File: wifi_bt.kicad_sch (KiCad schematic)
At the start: 37 parts, among them J3 U_FL-R-SMT-1, U26 WiFi_Bluetooth_LBEE5PK2AE, Y4 Oscillator_32.768kHz_ECS_2520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

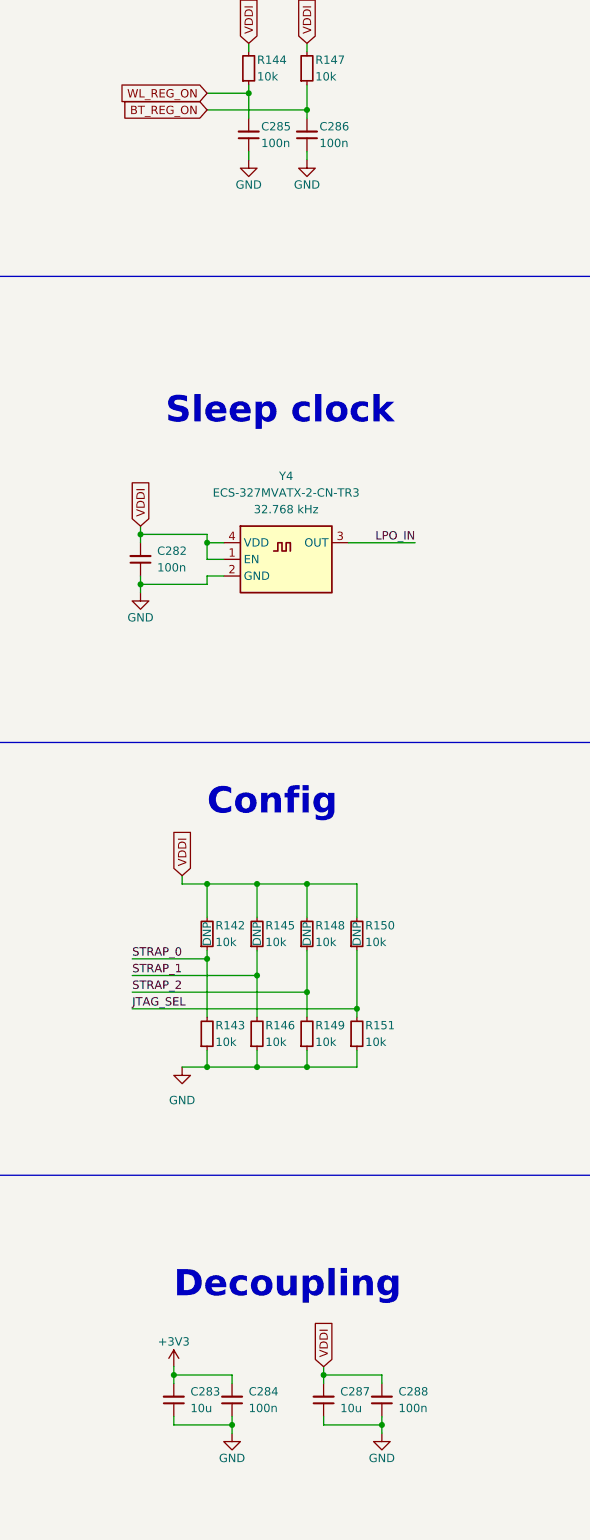
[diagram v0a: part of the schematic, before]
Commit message: [#55992] Move Flash and WL_BT module down
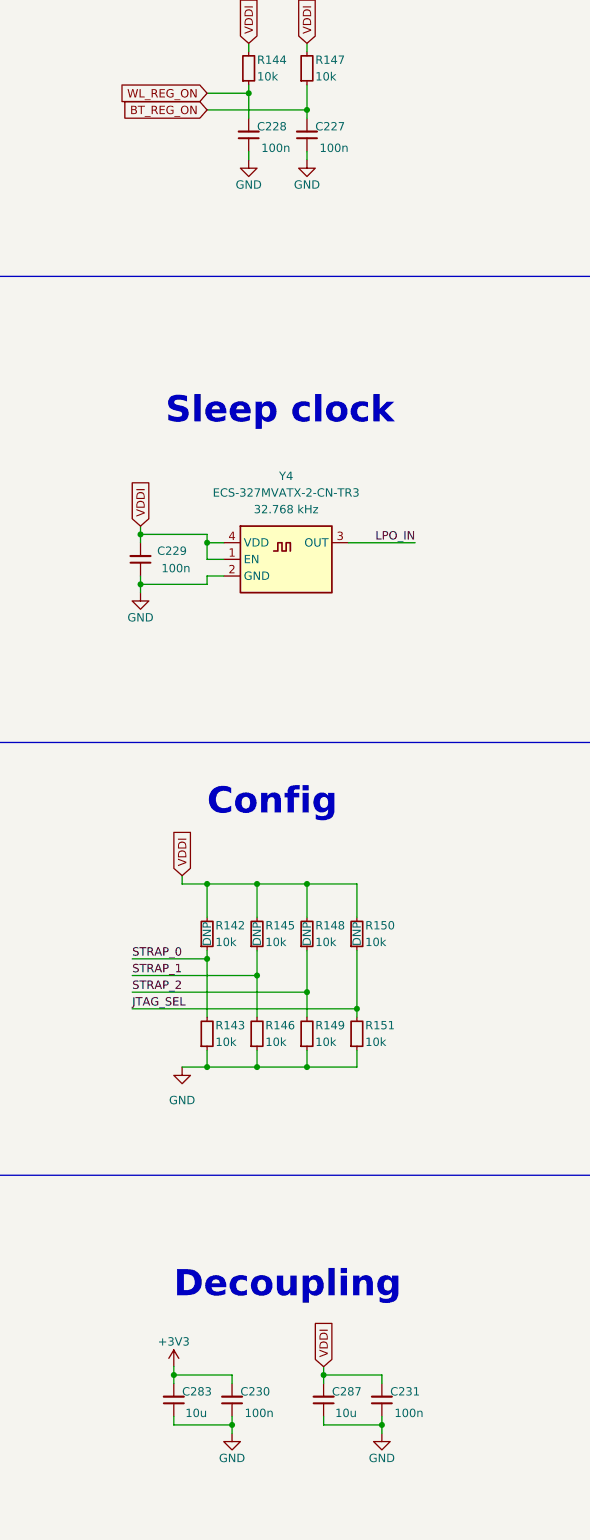
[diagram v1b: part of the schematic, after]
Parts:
- removed C282, C284, C285, C286, C288: C_100n_0201_25V, antmicro-footprints:C_0201, symbol antmicroCapacitorsmisc:C_100n_0201_25V
- added C227, C228, C229, C230, C231: C_100n_0402, antmicro-footprints:C_0402_1005Metric, symbol antmicroCapacitors0402:C_100n_0402
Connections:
- net +3V3: now also C230.2
- net BT_REG_ON: now also C227.2
- net GND: now also C227.1, C228.1, C229.1, C230.1, C231.1
- net VDDI: now also C229.2, C231.2
- net WL_REG_ON: now also C228.2

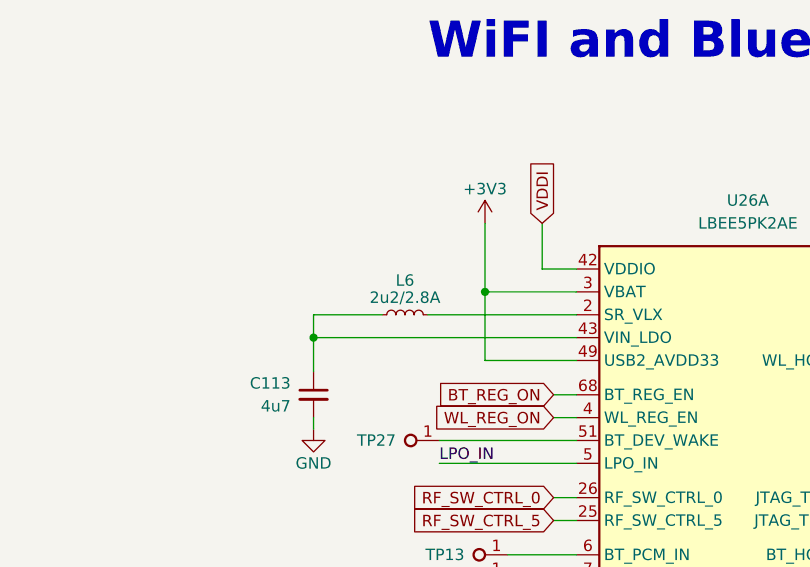
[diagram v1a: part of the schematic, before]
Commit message: [#56232] Replace WL_BT module's inductor
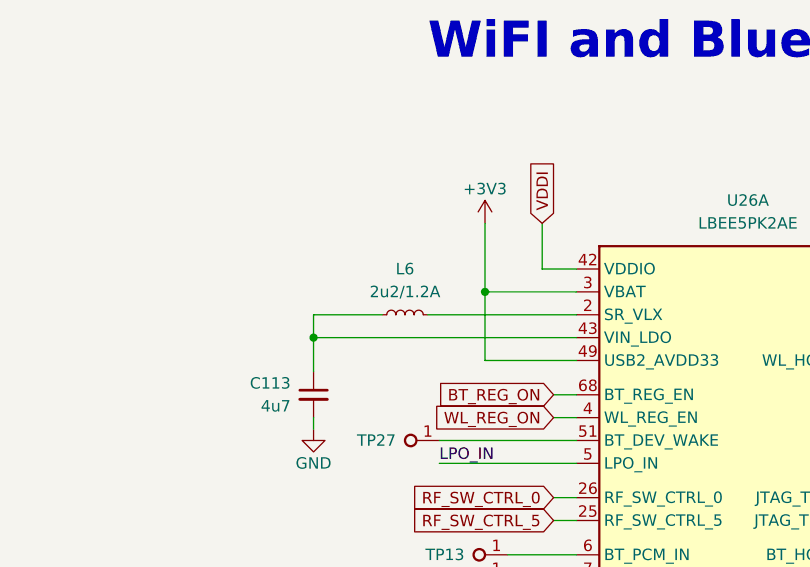
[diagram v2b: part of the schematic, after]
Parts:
- removed L6: L_2u2_2.8A_1008, antmicro-footprints:L_1008_2520Metric, symbol antmicroFixedInductors:L_2u2_2.8A_1008
- added L6: L_2u2_1.2A_0603_ABRACON-AOTA, antmicro-footprints:L_0603_1608Metric, symbol antmicroFixedInductors:L_2u2_1.2A_0603_Abracon-AOTA
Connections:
- net at C113.1, U26.43 (VIN_LDO): now also L6.1
- net at U26.2 (SR_VLX): now also L6.2
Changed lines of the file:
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@@
-    )
-  )
-  (symbol (lib_id "antmicroFixedInductors:L_2u2_2.8A_1008") (at 250.19 104.14 0) (unit 1)
-    (in_bom yes) (on_board yes) (dnp no)
-    (property "Reference" "L6" (at 252.73 100.33 0)
-      (effects (font (size 1.27 1.27) (thickness 0.15)))
-    )
-    (property "Value" "L_2u2_2.8A_1008" (at 264.16 106.68 0)
-      (effects (font (size 1.27 1.27) (thickness 0.15)) (justify left bottom) hide)
-    )
-    (property "Footprint" "antmicro-footprints:L_1008_2520Metric" (at 264.16 111.76 0)
-      (effects (font (size 1.27 1.27) (thickness 0.15)) (justify left bottom) hide)
-    )
-    (property "Datasheet" "https://product.tdk.com/en/search/inductor/inductor/smd/info?part_no=TFM252012ALMA2R2MTAA" (at 264.16 114.3 0)
-      (effects (font (size 1.27 1.27) (thickness 0.15)) (justify left bottom) hide)
-    )
-    (property "Val" "2u2/2.8A" (at 252.73 102.235 0)
-      (effects (font (size 1.27 1.27) (thickness 0.15)))
-    )
-    (property "Manufacturer" "TDK" (at 264.16 116.84 0)
-      (effects (font (size 1.27 1.27) (thickness 0.15)) (justify left bottom) hide)
-    )
-    (property "MPN" "TFM252012ALMA2R2MTAA" (at 264.16 119.38 0)
-      (effects (font (size 1.27 1.27) (thickness 0.15)) (justify left bottom) hide)
-    )
-    (property "ISat" "3.3 A" (at 264.16 120.65 0)
-      (effects (font (size 1.27 1.27)) (justify left) hide)
-    )
-    (property "IMax" "2.8 A" (at 264.16 124.46 0)
-      (effects (font (size 1.27 1.27) (thickness 0.15)) (justify left bottom) hide)
-    )
-    (property "Size" "2.5x2.0" (at 264.16 127 0)
-      (effects (font (size 1.27 1.27) (thickness 0.15)) (justify left bottom) hide)
-    )
-    (property "Author" "Antmicro" (at 264.16 129.54 0)
-      (effects (font (size 1.27 1.27) (thickness 0.15)) (justify left bottom) hide)
-    )
-    (property "License" "Apache-2.0" (at 264.16 132.08 0)
-      (effects (font (size 1.27 1.27) (thickness 0.15)) (justify left bottom) hide)
-    )
-    (pin "1")
-    (pin "2")
-    (instances
-      (project "polarfire-som"
-        (path "/db4a0d3e-2eb3-499e-977d-6eb378cfd3ed/8b90881e-9aeb-4751-9bcc-bff3e303e2ab"
-          (reference "L6") (unit 1)
-        )
-      )
     )
   )
@@
         )
       )
+    )
+  )
+  (symbol (lib_id "antmicroFixedInductors:L_2u2_1.2A_0603_Abracon-AOTA") (at 250.19 104.14 0) (unit 1)
+    (in_bom yes) (on_board yes) (dnp no) (fields_autoplaced)
+    (property "Reference" "L6" (at 252.73 99.06 0)
+      (effects (font (size 1.27 1.27) (thickness 0.15)))
+    )
+    (property "Value" "L_2u2_1.2A_0603_ABRACON-AOTA" (at 264.16 106.68 0)
+      (effects (font (size 1.27 1.27) (thickness 0.15)) (justify left bottom) hide)
+    )
+    (property "Footprint" "antmicro-footprints:L_0603_1608Metric" (at 264.16 111.76 0)
+      (effects (font (size 1.27 1.27) (thickness 0.15)) (justify left bottom) hide)
+    )
+    (property "Datasheet" "https://www.mouser.com/datasheet/2/3/AOTA_B160808S-3224144.pdf" (at 264.16 114.3 0)
+      (effects (font (size 1.27 1.27) (thickness 0.15)) (justify left bottom) hide)
+    )
+    (property "Val" "2u2/1.2A" (at 252.73 101.6 0)
+      (effects (font (size 1.27 1.27) (thickness 0.15)))
+    )
+    (property "Manufacturer" "Abracon" (at 264.16 116.84 0)
+      (effects (font (size 1.27 1.27) (thickness 0.15)) (justify left bottom) hide)
+    )
+    (property "MPN" "AOTA-B160808S2R2MT " (at 264.16 119.38 0)
+      (effects (font (size 1.27 1.27) (thickness 0.15)) (justify left bottom) hide)
+    )
+    (property "ISat" "1.3 A" (at 264.16 120.65 0)
+      (effects (font (size 1.27 1.27)) (justify left) hide)
+    )
+    (property "IMax" "1.2 A" (at 264.16 124.46 0)
+      (effects (font (size 1.27 1.27) (thickness 0.15)) (justify left bottom) hide)
+    )
+    (property "Size" "1.6 x 0.8 x 0.8" (at 264.16 127 0)
+      (effects (font (size 1.27 1.27) (thickness 0.15)) (justify left bottom) hide)
+    )
+    (property "Author" "Antmicro" (at 264.16 129.54 0)
+      (effects (font (size 1.27 1.27) (thickness 0.15)) (justify left bottom) hide)
+    )
+    (property "License" "Apache-2.0" (at 264.16 132.08 0)
+      (effects (font (size 1.27 1.27) (thickness 0.15)) (justify left bottom) hide)
+    )
+    (pin "2")
+    (pin "1")
+    (instances
+      (project "polarfire-som"
+        (path "/db4a0d3e-2eb3-499e-977d-6eb378cfd3ed/8b90881e-9aeb-4751-9bcc-bff3e303e2ab"
+          (reference "L6") (unit 1)
+        )
+      )

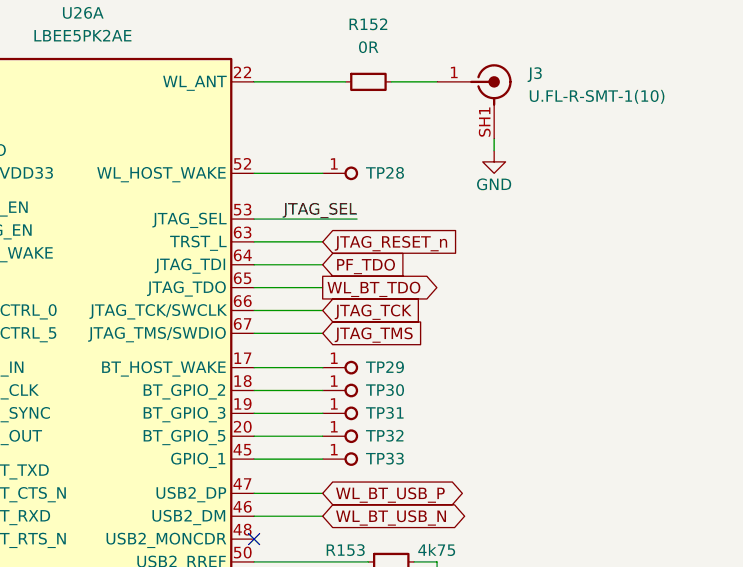
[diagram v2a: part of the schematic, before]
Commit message: [#56466] Remove I2C selector and JTAG chain
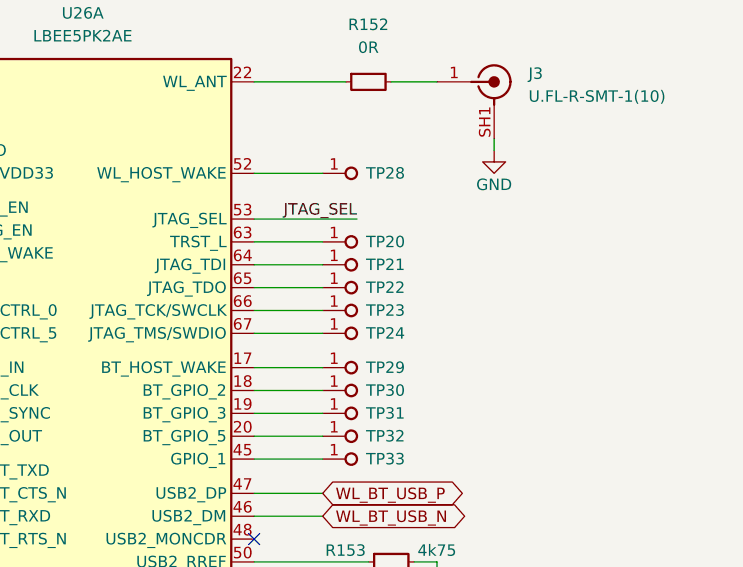
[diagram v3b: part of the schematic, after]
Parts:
- added TP20, TP21, TP22, TP23, TP24: TP_0.75mm_SMD, antmicro-footprints:TP_SMD_0.75mm, symbol antmicroTestPoints:TP_0.75mm_SMD
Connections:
- net JTAG_RESET_n: no longer names the net of U26.63 (TRST_L)
- net JTAG_RESET_n: now also TP20.1
- net JTAG_TCK: no longer names the net of U26.66 (JTAG_TCK/SWCLK)
- net JTAG_TCK: now also TP23.1
- net JTAG_TMS: no longer names the net of U26.67 (JTAG_TMS/SWDIO)
- net JTAG_TMS: now also TP24.1
- net PF_TDO: no longer names the net of U26.64 (JTAG_TDI)
- net PF_TDO: now also TP21.1
- net WL_BT_TDO: no longer names the net of U26.65 (JTAG_TDO)
- net WL_BT_TDO: now also TP22.1

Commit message: [#56466] Add Edge-Connect, restore JTAG chain
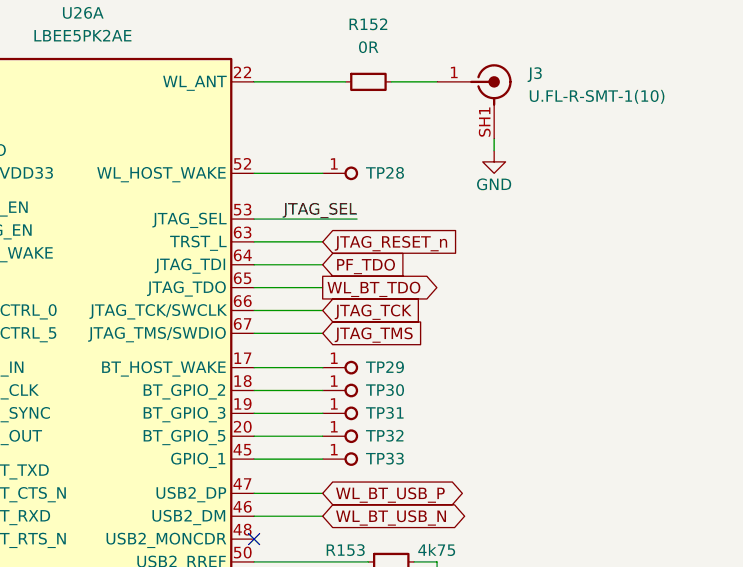
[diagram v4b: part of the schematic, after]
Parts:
- removed TP20, TP21, TP22, TP23, TP24: TP_0.75mm_SMD, antmicro-footprints:TP_SMD_0.75mm, symbol antmicroTestPoints:TP_0.75mm_SMD
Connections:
- net JTAG_RESET_n: now reaches U26.63 (TRST_L)
- net PF_TDO: now reaches U26.64 (JTAG_TDI)
- net WL_BT_TDO: now reaches U26.65 (JTAG_TDO)
- net JTAG_TCK: now reaches U26.66 (JTAG_TCK/SWCLK)
- net JTAG_TMS: now reaches U26.67 (JTAG_TMS/SWDIO)

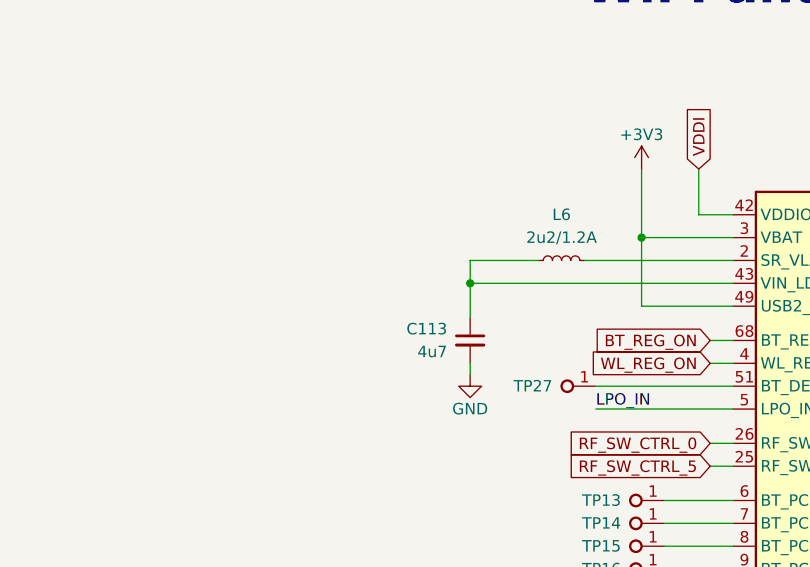
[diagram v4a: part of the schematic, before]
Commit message: [#56952] Place top designators, clean ERC
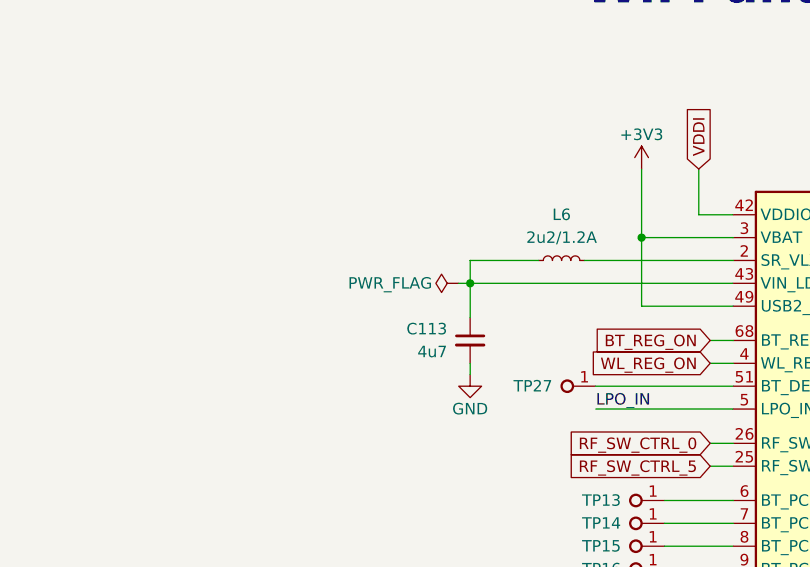
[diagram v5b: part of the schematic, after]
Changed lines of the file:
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@@
+    (stroke (width 0) (type default))
+  )
+  (wire (pts (xy 241.3 106.68) (xy 242.57 106.68))
     (stroke (width 0) (type default))
   )
@@
         )
       )
+    )
+  )
+  (symbol (lib_id "antmicropower:PWR_FLAG") (at 241.3 106.68 90) (unit 1)
+    (in_bom yes) (on_board yes) (dnp no)
+    (property "Reference" "#FLG023" (at 239.395 106.68 0)
+      (effects (font (size 1.27 1.27)) hide)
+    )
+    (property "Value" "PWR_FLAG" (at 233.68 106.68 90)
+      (effects (font (size 1.27 1.27)))
+    )
+    (property "Footprint" "" (at 241.3 106.68 0)
+      (effects (font (size 1.27 1.27)) hide)
+    )
+    (property "Datasheet" "" (at 241.3 106.68 0)
+      (effects (font (size 1.27 1.27)) hide)
+    )
+    (pin "1")
+    (instances
+      (project "polarfire-som"
+        (path "/db4a0d3e-2eb3-499e-977d-6eb378cfd3ed/8b90881e-9aeb-4751-9bcc-bff3e303e2ab"
+          (reference "#FLG023") (unit 1)
+        )
+      )

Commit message: Update components
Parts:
- L6: value L_2u2_1.2A_0603_ABRACON-AOTA -> L_2u2_1.2A_0603; symbol antmicroFixedInductors:L_2u2_1.2A_0603_Abracon-AOTA -> antmicroFixedInductors:L_2u2_1.2A_0603
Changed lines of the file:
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@@
     )
   )
-  (symbol (lib_id "antmicroFixedInductors:L_2u2_1.2A_0603_Abracon-AOTA") (at 250.19 104.14 0) (unit 1)
+  (symbol (lib_id "antmicroFixedInductors:L_2u2_1.2A_0603") (at 250.19 104.14 0) (unit 1)
     (in_bom yes) (on_board yes) (dnp no) (fields_autoplaced)
     (property "Reference" "L6" (at 252.73 99.06 0)
       (effects (font (size 1.27 1.27) (thickness 0.15)))
     )
-    (property "Value" "L_2u2_1.2A_0603_ABRACON-AOTA" (at 264.16 106.68 0)
+    (property "Value" "L_2u2_1.2A_0603" (at 264.16 106.68 0)
       (effects (font (size 1.27 1.27) (thickness 0.15)) (justify left bottom) hide)
     )

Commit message: [#57422] Update DNP
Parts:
- R142, R145, R148, R150: now not fitted
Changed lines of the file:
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@@
   )
   (symbol (lib_id "antmicroResistors0402:R_10k_0402") (at 82.55 177.8 90) (unit 1)
-    (in_bom yes) (on_board yes) (dnp no)
+    (in_bom yes) (on_board yes) (dnp yes)
     (property "Reference" "R145" (at 83.82 173.99 90)
       (effects (font (size 1.27 1.27) (thickness 0.15)) (justify right))
@@
     )
     (property "DNP" "DNP" (at 82.55 175.26 0)
-      (effects (font (size 1.27 1.27)))
+      (effects (font (size 1.27 1.27)) hide)
     )
     (pin "1")
@@
   )
   (symbol (lib_id "antmicroResistors0402:R_10k_0402") (at 97.79 177.8 90) (unit 1)
-    (in_bom yes) (on_board yes) (dnp no)
+    (in_bom yes) (on_board yes) (dnp yes)
     (property "Reference" "R150" (at 99.06 173.99 90)
       (effects (font (size 1.27 1.27) (thickness 0.15)) (justify right))
@@
     )
     (property "DNP" "DNP" (at 97.79 175.26 0)
-      (effects (font (size 1.27 1.27)))
+      (effects (font (size 1.27 1.27)) hide)
     )
     (pin "1")
@@
   )
   (symbol (lib_id "antmicroResistors0402:R_10k_0402") (at 90.17 177.8 90) (unit 1)
-    (in_bom yes) (on_board yes) (dnp no)
+    (in_bom yes) (on_board yes) (dnp yes)
     (property "Reference" "R148" (at 91.44 173.99 90)
       (effects (font (size 1.27 1.27) (thickness 0.15)) (justify right))
@@
     )
     (property "DNP" "DNP" (at 90.17 175.26 0)
-      (effects (font (size 1.27 1.27)))
+      (effects (font (size 1.27 1.27)) hide)
     )
     (pin "1")
@@
   )
   (symbol (lib_id "antmicroResistors0402:R_10k_0402") (at 74.93 177.8 90) (unit 1)
-    (in_bom yes) (on_board yes) (dnp no)
+    (in_bom yes) (on_board yes) (dnp yes)
     (property "Reference" "R142" (at 76.2 173.99 90)
       (effects (font (size 1.27 1.27) (thickness 0.15)) (justify right))
@@
     )
     (property "DNP" "DNP" (at 74.93 175.26 0)
-      (effects (font (size 1.27 1.27)))
-    )
-    (pin "1")
+      (effects (font (size 1.27 1.27)) hide)
+    )
+    (pin "1")
